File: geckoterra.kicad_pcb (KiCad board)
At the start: 2 copper layers, 22 parts, among them J1 Conn_WallSocket_Earth, J6 Conn_01x02, J7 Conn_01x02, J8 Conn_01x02, P1 Conn_WallPlug_Earth, Q1 2N3904, Q2 Q_NMOS_GDS, U1 PC817, U2 4N25

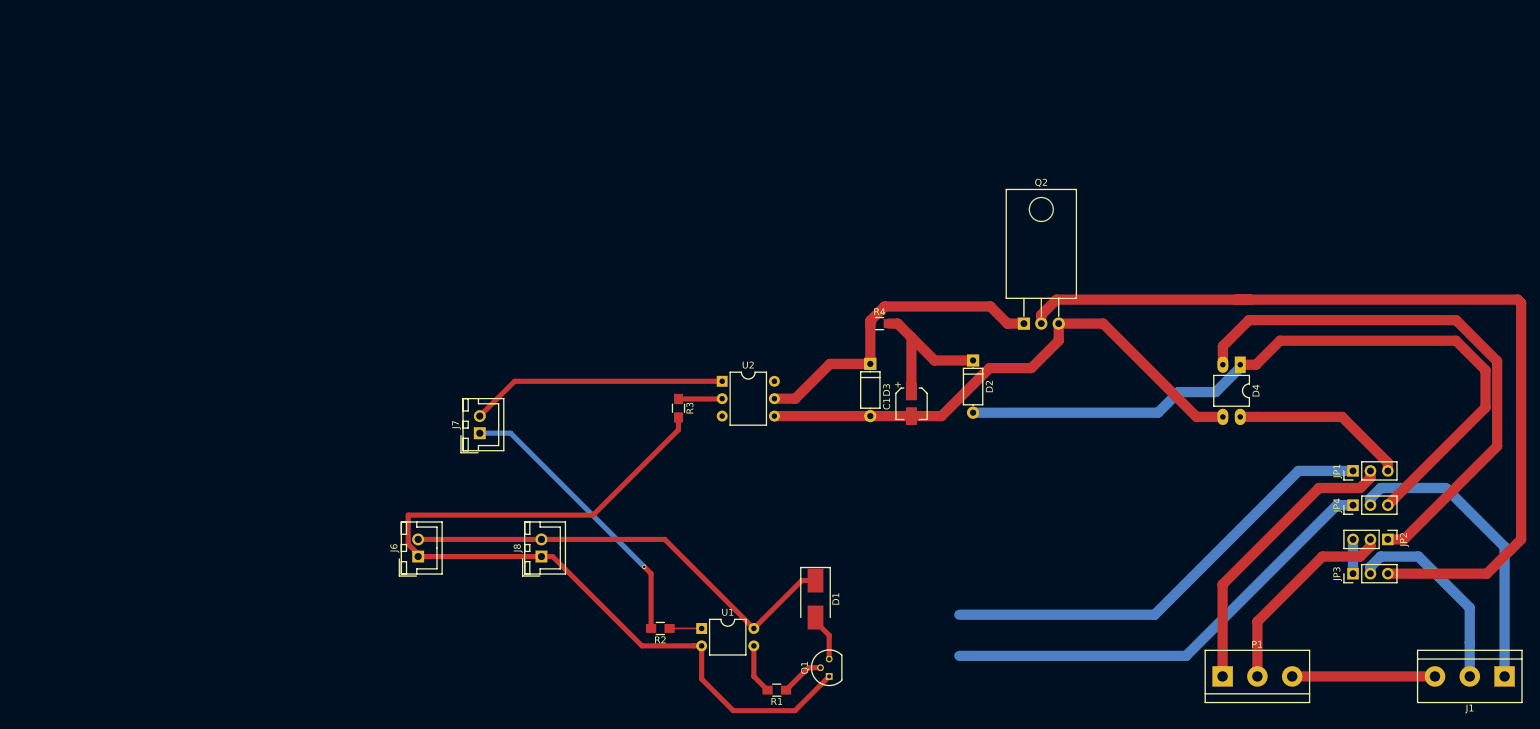
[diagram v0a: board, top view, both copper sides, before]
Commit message: Fix footprint of relay. Create a first version 5x5cm board.
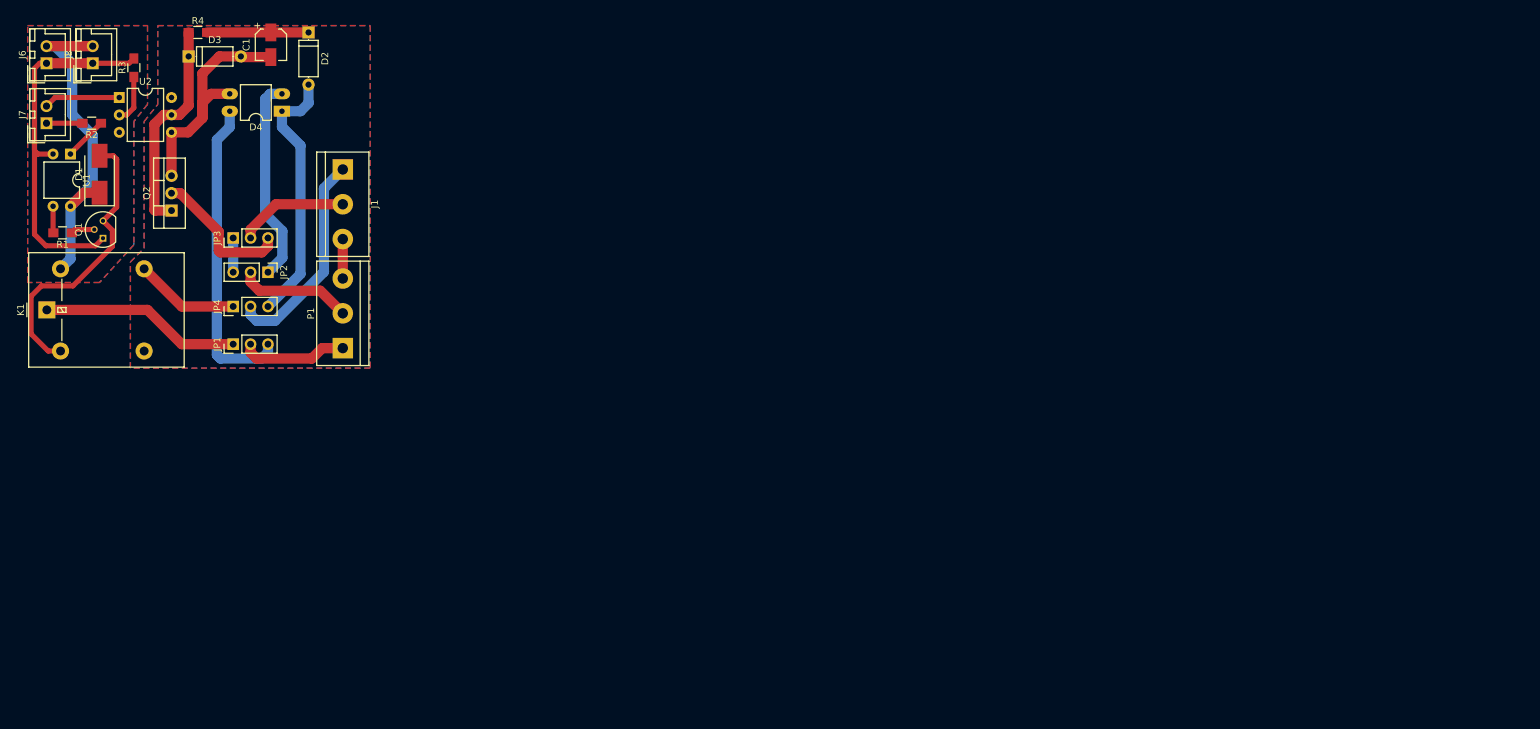
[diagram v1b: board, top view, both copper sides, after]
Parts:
- added K1: SANYOU_SRD_Form_A, Relays_THT:Relay_SPDT_OMRON-G5LE-1, F.Cu at (52.8, 91.5)
- Q2: footprint TO_SOT_Packages_THT:TO-220-3_Horizontal -> TO_SOT_Packages_THT:TO-220-3_Vertical
- moved J1 185.0 mm to (96.0, 71.0), turned to 270 degrees
- moved JP3 170.6 mm to (80.0, 81.0)
- moved JP2 168.0 mm to (85.1, 86.0)
- moved JP4 166.0 mm to (80.0, 91.0)
- moved JP1 164.5 mm to (80.0, 96.5)
- moved D4 144.7 mm to (87.1, 62.5), turned to 180 degrees
- moved P1 137.1 mm to (96.0, 97.1), turned to 90 degrees
- moved Q2 125.5 mm to (71.0, 77.0), turned to 90 degrees
- moved Q1 123.8 mm to (61.0, 81.0)
- moved R1 123.8 mm to (55.1, 80.2)
- moved D1 121.5 mm to (60.5, 71.7), turned to 90 degrees
- moved U1 115.3 mm to (56.2, 68.8), turned to 270 degrees
- moved R2 111.0 mm to (59.4, 64.2)
- moved D3 109.2 mm to (73.5, 54.5), turned to 0 degrees
- moved R4 108.2 mm to (74.8, 51.0)
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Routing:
- net Net-(JP3-Pad3): track 130.5 -> 20.9 mm
- net GND: track 127.3 -> 56.6 mm
- net Net-(D2-Pad2): track 106.8 -> 38.7 mm
- net Net-(JP4-Pad1): track 66.6 -> 15.3 mm
- net Net-(D4-Pad2): track 80.8 -> 30.0 mm
- net Net-(C1-Pad2): track 78.2 -> 36.1 mm
- net Net-(JP1-Pad1): track 66.2 -> 29.3 mm
- net /RelayPin: track 41.5 -> 5.25 mm, vias 1 -> 0
- net Net-(D1-Pad2): track 6.89 -> 42.6 mm
- net Net-(JP1-Pad2): track 42.5 -> 15.7 mm
- net /PWMPin: track 37.5 -> 11.1 mm
- net Net-(D4-Pad4): track 25.5 -> 45.6 mm
- net +5V: track 66.3 -> 49.8 mm
- net Net-(J1-Pad3): track 20.8 -> 5.76 mm
- net Net-(D3-Pad1): track 46.7 -> 31.8 mm
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- added copper zone on B.Cu, net GND
- added copper zone on F.Cu, net GND
- added copper zone on B.Cu, net Net-(J1-Pad3)
- added copper zone on F.Cu, net Net-(J1-Pad3)
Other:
- net class AC: clearance 0.2 -> 0.5
- net class Default: clearance 0.2 -> 0.5
- net class Power: clearance 0.2 -> 0.5
- rule trace_clearance: 0.2 -> 0.5

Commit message: edge cuts
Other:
- board outline added: 50 x 50 mm
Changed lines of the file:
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@@
     (area 47.725 48.025 102.455 103.142858)
     (thickness 1.6)
-    (drawings 4)
+    (drawings 8)
     (tracks 122)
     (zones 0)
@@
     )
   )
+  (gr_line (start 50 100) (end 50 50) (layer Edge.Cuts) (width 0.15))
+  (gr_line (start 100 100) (end 50 100) (layer Edge.Cuts) (width 0.15))
+  (gr_line (start 100 50) (end 100 100) (layer Edge.Cuts) (width 0.15))
+  (gr_line (start 50 50) (end 100 50) (layer Edge.Cuts) (width 0.15))
   (gr_line (start 50 100) (end 50 50) (layer Dwgs.User) (width 0.2))
   (gr_line (start 100 100) (end 50 100) (layer Dwgs.User) (width 0.2))

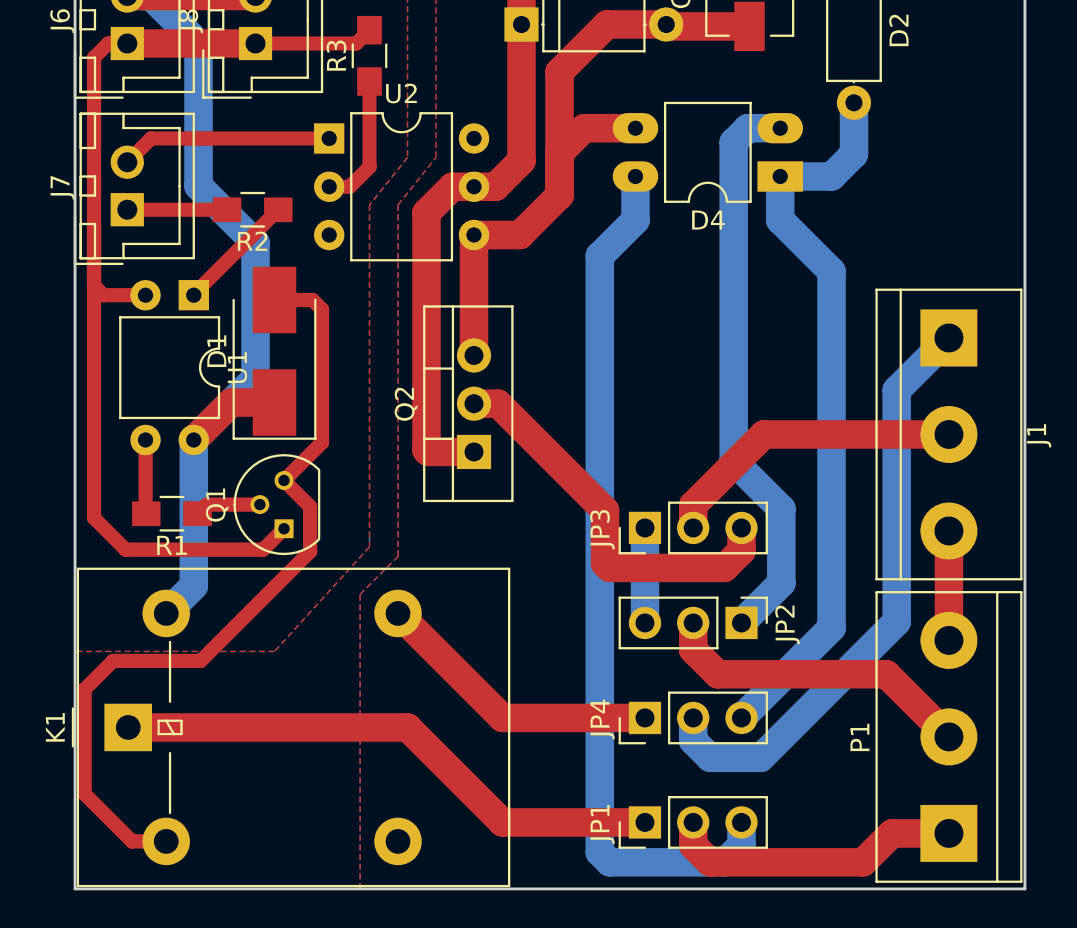
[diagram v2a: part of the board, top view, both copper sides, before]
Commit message: Use jumper resistors instead of a switch. update pcb.
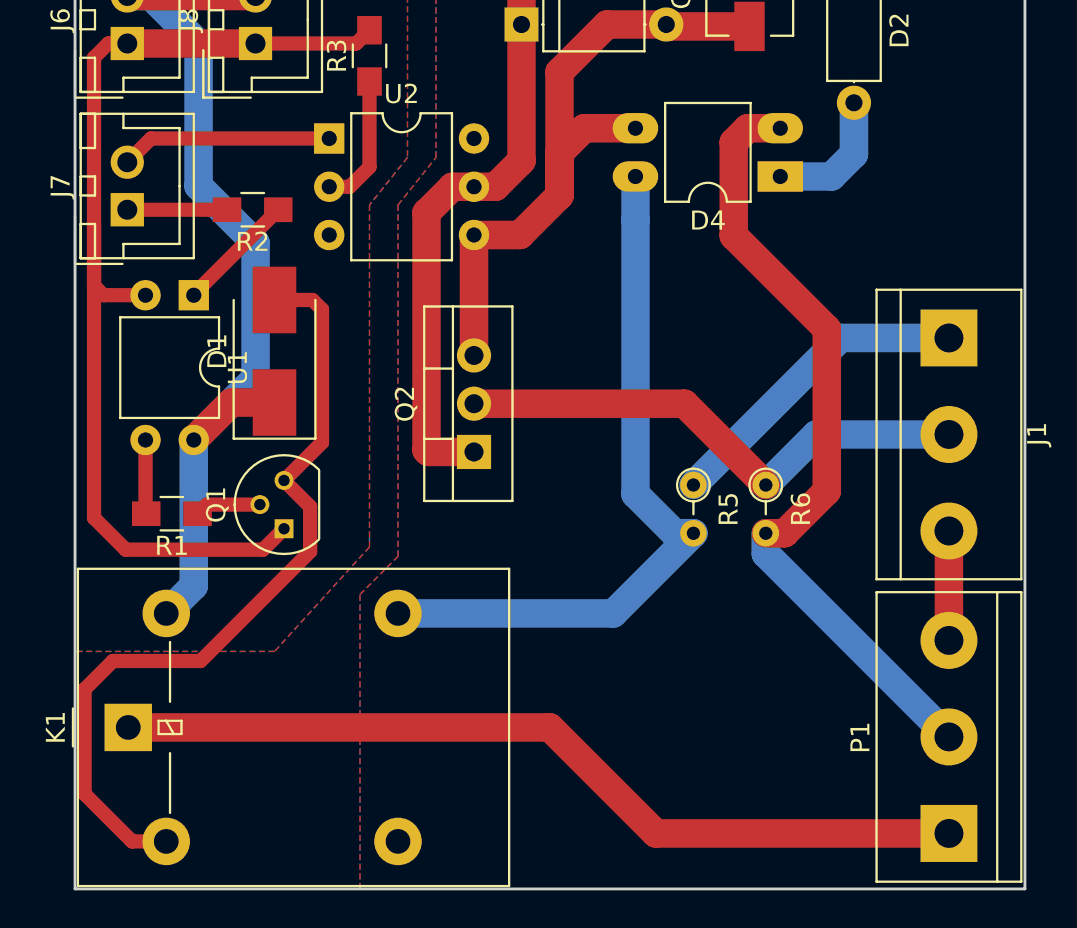
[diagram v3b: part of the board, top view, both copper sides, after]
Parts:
- removed JP1, JP2, JP3, JP4: Jumper_NC_Dual, Pin_Headers:Pin_Header_Straight_1x03_Pitch2.54mm
- added R5: Shunt, Resistors_THT:R_Axial_DIN0204_L3.6mm_D1.6mm_P2.54mm_Vertical, F.Cu at (82.5, 78.7)
- added R6: Shunt, Resistors_THT:R_Axial_DIN0204_L3.6mm_D1.6mm_P2.54mm_Vertical, F.Cu at (86.4, 78.7)
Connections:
- J1 pad 1: Net-(J1-Pad1) -> Net-(D2-Pad2)
- K1 pad 1: Net-(JP1-Pad1) -> Net-(K1-Pad1)
- K1 pad 4: Net-(JP4-Pad1) -> Net-(D4-Pad4)
- P1 pad 1: Net-(JP1-Pad2) -> Net-(K1-Pad1)
- P1 pad 2: Net-(JP2-Pad2) -> Net-(D4-Pad2)
- Q2 pad 2: Net-(JP3-Pad3) -> Net-(J1-Pad2)
- U2 pad 3: Net-(U2-Pad3) -> (no net)
- U2 pad 6: Net-(U2-Pad6) -> (no net)
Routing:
- net Net-(K1-Pad1): track 0.00 -> 45.5 mm
- net Net-(J1-Pad1): track 31.3 -> 0.00 mm
- net Net-(JP1-Pad1): track 29.3 -> 0.00 mm
- net Net-(JP3-Pad3): track 20.9 -> 0.00 mm
- net Net-(JP2-Pad2): track 16.8 -> 0.00 mm
- net Net-(JP1-Pad2): track 15.7 -> 0.00 mm
- net Net-(JP4-Pad1): track 15.3 -> 0.00 mm
- net Net-(D2-Pad2): track 38.7 -> 23.7 mm
- net Net-(D4-Pad2): track 30.0 -> 42.0 mm
- net Net-(J1-Pad2): track 16.2 -> 27.9 mm
- net Net-(D4-Pad4): track 45.6 -> 37.9 mm
- net Net-(JP2-Pad3): track 5.00 -> 0.00 mm

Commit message: update pcb
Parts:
- moved K1 10.0 mm to (62.8, 91.5)
- moved P1 9.56 mm to (86.5, 96.0), turned to 0 degrees
- moved J1 9.50 mm to (96.0, 80.5), turned to 90 degrees
- moved R5 5.13 mm to (87.5, 80.0), turned to 180 degrees
- moved R6 3.92 mm to (87.5, 75.0), turned to 180 degrees
- moved C1 2.69 mm to (88.0, 53.8)
- moved D2 2.69 mm to (93.5, 52.0)
- moved D3 2.69 mm to (76.0, 55.5)
- moved D4 2.69 mm to (89.6, 63.5)
- moved R4 2.69 mm to (77.3, 52.0)
- moved Q2 2.50 mm to (73.5, 77.0)
- moved U2 2.50 mm to (65.9, 60.5)
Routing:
- net GND: track 56.6 -> 82.9 mm
- net Net-(J1-Pad3): track 5.76 -> 27.7 mm
- net Net-(K1-Pad1): track 45.5 -> 27.3 mm
- net Net-(D2-Pad2): track 23.7 -> 36.4 mm
- net Net-(D4-Pad4): track 37.9 -> 29.0 mm
- net Net-(D1-Pad2): track 42.6 -> 34.5 mm
- net +5V: track 49.8 -> 57.1 mm
- net Net-(D3-Pad1): track 31.8 -> 35.0 mm
- net Net-(J1-Pad2): track 27.9 -> 25.3 mm
- net /PWMPin: track 11.1 -> 13.6 mm
- net Net-(C1-Pad2): track 36.1 -> 34.3 mm
- net Net-(R3-Pad1): track 7.05 -> 8.57 mm
- net Net-(D4-Pad2): track 42.0 -> 43.2 mm

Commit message: Update pcb, again. Kinda finished.
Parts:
- moved J8 41.6 mm to (56.0, 97.0), turned to 180 degrees
- moved J6 3.58 mm to (56.0, 54.0), turned to 180 degrees
- moved D1 1.25 mm to (61.8, 71.7)
- moved J7 1.25 mm to (54.0, 64.2)
- moved R1 1.25 mm to (56.4, 80.2)
- moved R2 1.25 mm to (60.6, 64.2)
- moved U1 1.25 mm to (57.5, 68.8)
- moved Q1 0.79 mm to (61.0, 80.2), turned to 0 degrees
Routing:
- net +5V: track 57.1 -> 79.2 mm
- net GND: track 82.9 -> 80.5 mm
- net Net-(D1-Pad2): track 34.5 -> 36.9 mm
- net Net-(Q1-Pad2): track 3.48 -> 5.47 mm
- net Net-(D4-Pad4): track 29.0 -> 27.3 mm
- net /PWMPin: track 13.6 -> 12.4 mm
- net Net-(J1-Pad2): track 25.3 -> 26.4 mm
